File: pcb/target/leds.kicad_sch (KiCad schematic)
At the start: 0 parts

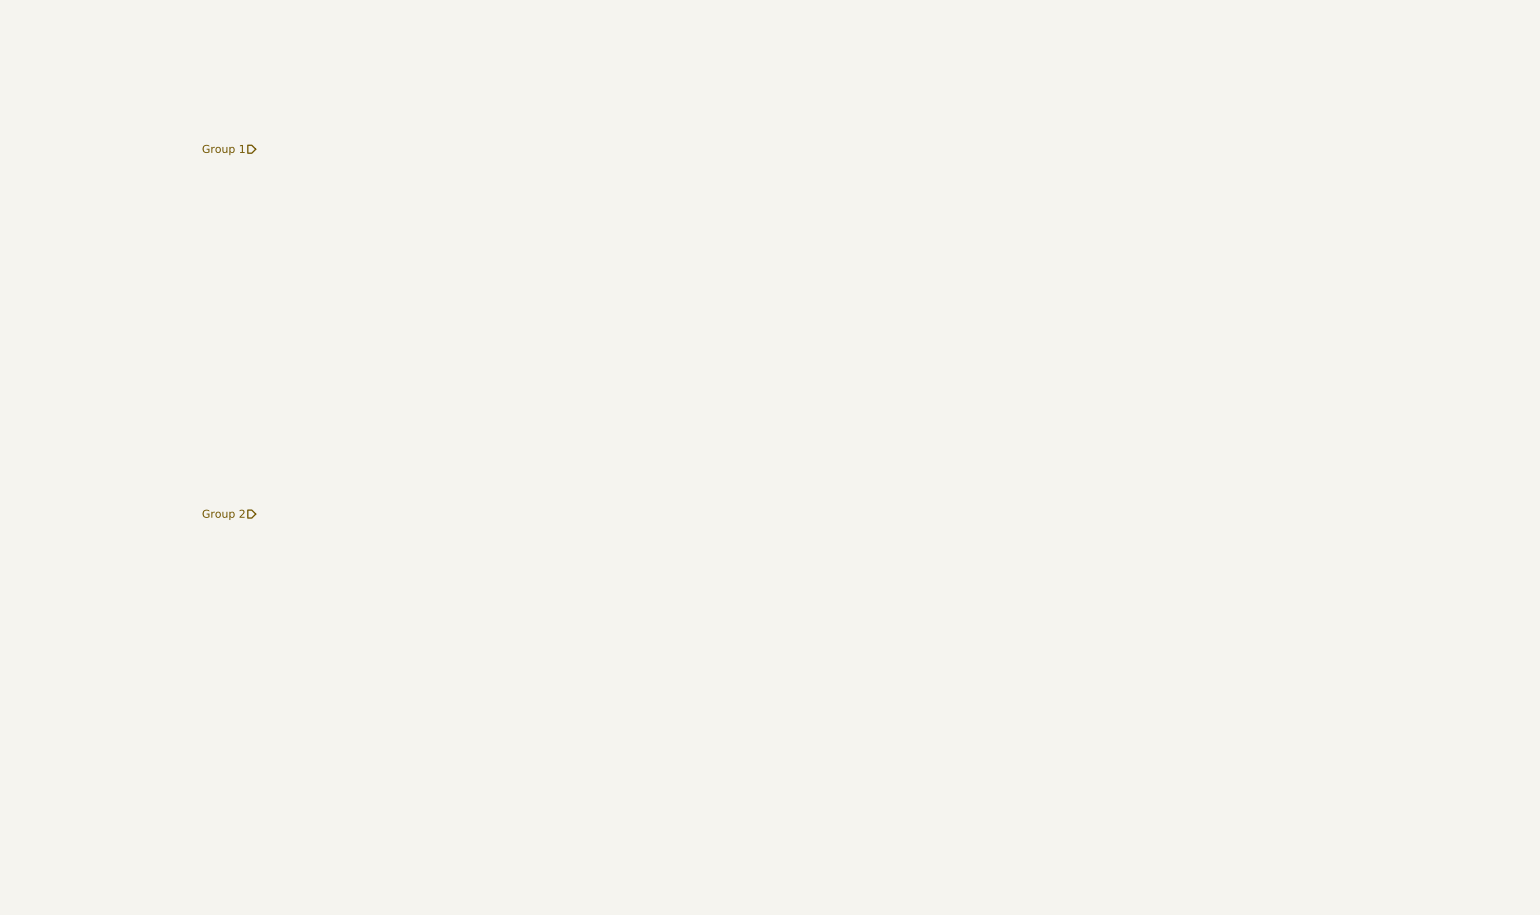
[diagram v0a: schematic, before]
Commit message: First iteration of target schematic
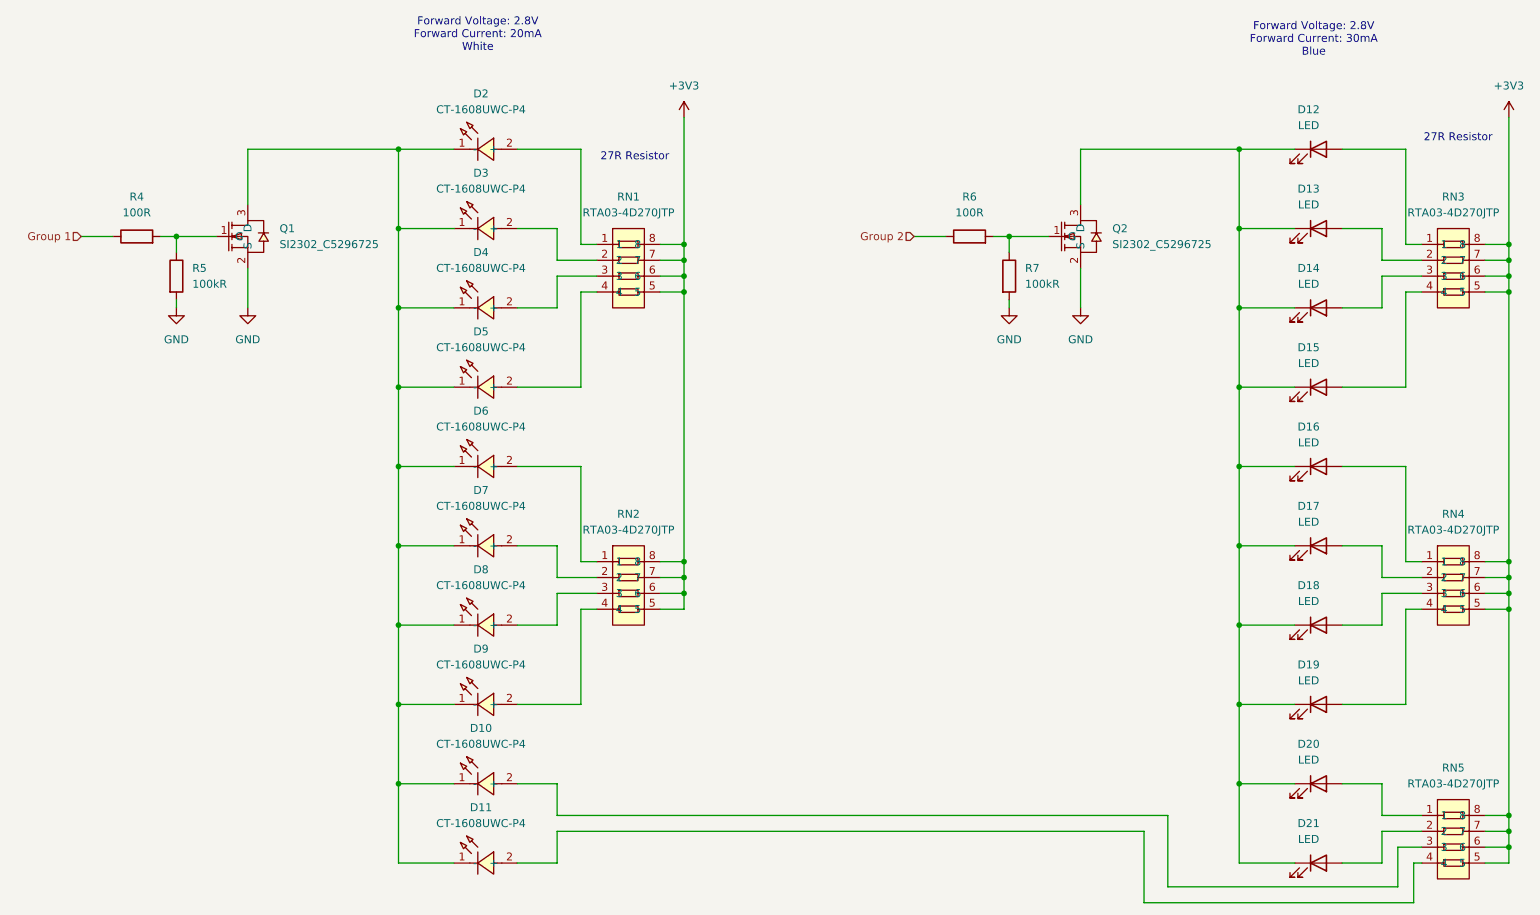
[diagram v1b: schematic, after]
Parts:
- added D10, D11, D2, D3, D4, D5, D6, D7, D8, D9: CT-1608UWC-P4, lcsc:LED-SMD_L1.6-W0.8-RD_CT-1608UWC-P4, symbol lcsc:CT-1608UWC-P4
- added D12, D13, D14, D15, D16, D17, D18, D19, D20, D21: LED, LED_SMD:LED_0603_1608Metric, symbol Device:LED
- added Q1, Q2: SI2302_C5296725, lcsc:SOT-23-3_L2.9-W1.3-P1.90-LS2.4-BR, symbol lcsc:SI2302_C5296725
- added R4, R6: 100R, Resistor_SMD:R_0603_1608Metric, symbol Device:R
- added R5, R7: 100kR, symbol Device:R
- added RN1, RN2, RN3, RN4, RN5: RTA03-4D270JTP, lcsc:RES-ARRAY-SMD_0603-8P-L3.2-W1.6-BL, symbol lcsc:RTA03-4D270JTP
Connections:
- net Group 1: now also R4.1
- net Group 2: now also R6.1
- new net: D12.1 (K), D13.1 (K), D14.1 (K), D15.1 (K), D16.1 (K), D17.1 (K), D18.1 (K), D19.1 (K), D20.1 (K), D21.1 (K), Q2.3 (D)
- new net: D14.2 (A), RN3.3
- new net: D20.2 (A), RN5.1
- new net: Q2.1 (G), R6.2, R7.1
- new net: D10.1 (-), D11.1 (-), D2.1 (-), D3.1 (-), D4.1 (-), D5.1 (-), D6.1 (-), D7.1 (-), D8.1 (-), D9.1 (-), Q1.3 (D)
- new net: D8.2 (+), RN2.3
- new net: D4.2 (+), RN1.3
- new net: D13.2 (A), RN3.2
- new net: D6.2 (+), RN2.1
- new net: D5.2 (+), RN1.4
- new net: Q1.1 (G), R4.2, R5.1
- new net: D2.2 (+), RN1.1
- new net: D17.2 (A), RN4.2
- new net: D18.2 (A), RN4.3
- new net: D9.2 (+), RN2.4
- new net: D21.2 (A), RN5.2
- new net: D10.2 (+), RN5.3
- new net: D11.2 (+), RN5.4
- new net: D12.2 (A), RN3.1
- new net: D7.2 (+), RN2.2
- new net: D16.2 (A), RN4.1
- new net: D15.2 (A), RN3.4
- new net: D19.2 (A), RN4.4
- new net: D3.2 (+), RN1.2
- new net +3V3: RN1.5, RN1.6, RN1.7, RN1.8, RN2.5, RN2.6, RN2.7, RN2.8, RN3.5, RN3.6, RN3.7, RN3.8, RN4.5, RN4.6, RN4.7, RN4.8, RN5.5, RN5.6, RN5.7, RN5.8
- new net GND: Q1.2 (S), Q2.2 (S), R5.2, R7.2
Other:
- note added: "27R Resistor"
- note added: "Forward Voltage: 2.8V Forward Current: 20mA White"
- note added: "Forward Voltage: 2.8V Forward Current: 30mA Blue"

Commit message: Started controller schematic
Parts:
- removed D10, D11: CT-1608UWC-P4, lcsc:LED-SMD_L1.6-W0.8-RD_CT-1608UWC-P4, symbol lcsc:CT-1608UWC-P4
- removed D20, D21: LED, LED_SMD:LED_0603_1608Metric, symbol Device:LED
- removed RN5: RTA03-4D270JTP, lcsc:RES-ARRAY-SMD_0603-8P-L3.2-W1.6-BL, symbol lcsc:RTA03-4D270JTP
